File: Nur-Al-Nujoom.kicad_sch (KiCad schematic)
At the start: 0 parts

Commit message: sch done open for review
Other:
- added sheet Power Managment (Power Managment .kicad_sch)
- added sheet Switch (Switch.kicad_sch)
- sheet MCU ports: added PA0, PA1, PA10, PA2, PA3, PA4, PA5, PA6, PA7, PA8, PA9, PB0, PB1, PB10, PB11, PB12, PB13, PB14, PB15, PB2, VCC_3v3; removed none
- title: (none) -> Nur-Al-Nujoom

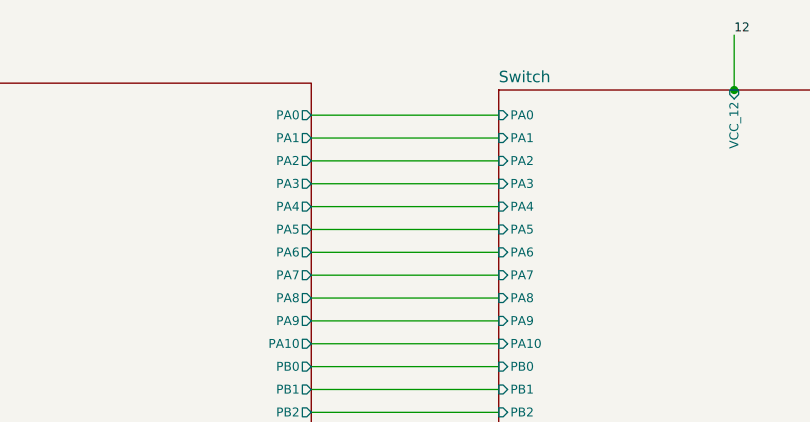
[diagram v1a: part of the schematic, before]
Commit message: updated Routing
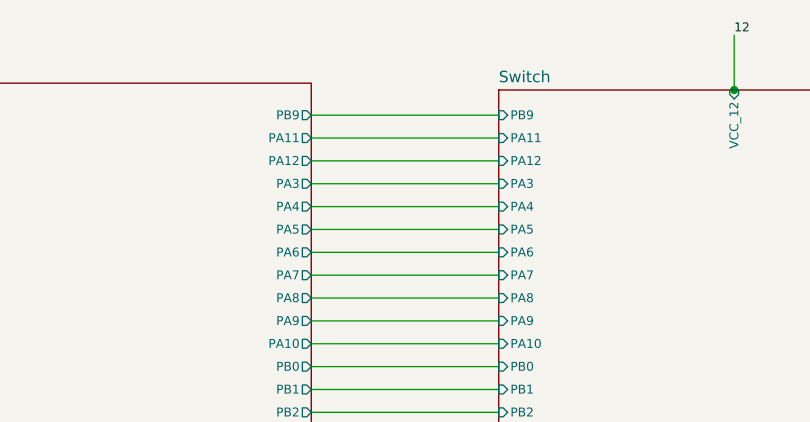
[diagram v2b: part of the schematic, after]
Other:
- sheet MCU ports: added PA11, PA12, PB9; removed PA0, PA1, PA2
- sheet Switch ports: added PA11, PA12, PB9; removed PA0, PA1, PA2
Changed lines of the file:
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@@
-			)
-		)
-		(pin "PA2" input
-			(at 194.818 59.69 180)
-			(effects
-				(font
-					(size 0.9906 0.9906)
-				)
-				(justify left)
 			)
 		)
@@
 			)
 		)
-		(pin "PA0" input
-			(at 194.818 54.61 180)
-			(effects
-				(font
-					(size 0.9906 0.9906)
-				)
-				(justify left)
-			)
-		)
-		(pin "PA1" input
-			(at 194.818 57.15 180)
-			(effects
-				(font
-					(size 0.9906 0.9906)
-				)
-				(justify left)
-			)
-		)
 		(pin "PA5" input
 			(at 194.818 67.31 180)
@@
 		(pin "PB10" input
 			(at 194.818 90.17 180)
+			(effects
+				(font
+					(size 0.9906 0.9906)
+				)
+				(justify left)
+			)
+		)
+		(pin "PA11" input
+			(at 194.818 57.15 180)
+			(effects
+				(font
+					(size 0.9906 0.9906)
+				)
+				(justify left)
+			)
+		)
+		(pin "PA12" input
+			(at 194.818 59.69 180)
+			(effects
+				(font
+					(size 0.9906 0.9906)
+				)
+				(justify left)
+			)
+		)
+		(pin "PB9" input
+			(at 194.818 54.61 180)
 			(effects
 				(font
@@
 			)
 		)
-		(pin "PA1" output
-			(at 173.99 57.15 0)
-			(effects
-				(font
-					(size 0.9906 0.9906)
-				)
-				(justify right)
-			)
-		)
-		(pin "PA0" output
-			(at 173.99 54.61 0)
-			(effects
-				(font
-					(size 0.9906 0.9906)
-				)
-				(justify right)
-			)
-		)
-		(pin "PA2" output
-			(at 173.99 59.69 0)
-			(effects
-				(font
-					(size 0.9906 0.9906)
-				)
-				(justify right)
-			)
-		)
 		(pin "PA3" output
 			(at 173.99 62.23 0)
@@
 			)
 		)
+		(pin "PA11" output
+			(at 173.99 57.15 0)
+			(effects
+				(font
+					(size 0.9906 0.9906)
+				)
+				(justify right)
+			)
+		)
+		(pin "PA12" output
+			(at 173.99 59.69 0)
+			(effects
+				(font
+					(size 0.9906 0.9906)
+				)
+				(justify right)
+			)
+		)
+		(pin "PB9" output
+			(at 173.99 54.61 0)
+			(effects
+				(font
+					(size 0.9906 0.9906)
+				)
+				(justify right)
+			)
+		)
